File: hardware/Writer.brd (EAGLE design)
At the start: 68.6 x 53.3 mm, 20 parts, among them CN1 IRKit Wifi, IC1 JAPANINO-SLIM, SW1 SS12D01G4, SW2 SLIDE-SWITCH4/2

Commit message: SW2's pin4 wasn't connected to GND
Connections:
- removed net N$8: SW2.4
- net GND: now also SW2.4
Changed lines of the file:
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@@
 <via x="62.7" y="24.2" extent="1-16" drill="0.4"/>
 <via x="6.6" y="44.1" extent="1-16" drill="0.4"/>
+<contactref element="SW2" pad="4"/>
+<wire x1="62.95" y1="20.37" x2="62.7" y2="20.37" width="0.4064" layer="1"/>
 </signal>
 <signal name="VIN">
@@
 <contactref element="SW2" pad="2"/>
 </signal>
-<signal name="N$8">
-<contactref element="SW2" pad="4"/>
-</signal>
 <signal name="N$9">

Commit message: better error handling and logs preparing for factory-checker firmware POWER switch disconnects 5V and GND when turned off methods for factory checker test script follows main changes
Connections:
- new net N$8: SW1.3
- net GND: no longer SW1.3
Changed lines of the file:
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@@
 <contactref element="ICSP" pad="6"/>
 <contactref element="CN1" pad="8"/>
-<contactref element="SW1" pad="3"/>
 <contactref element="JP1" pad="1"/>
 <contactref element="LED2" pad="K"/>
@@
 <wire x1="7.1" y1="13.5" x2="7.05" y2="13.5" width="0.254" layer="1"/>
 </signal>
+<signal name="N$8">
+<contactref element="SW1" pad="3"/>
+</signal>
 </signals>

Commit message: looks fine
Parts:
- removed ICSP: IRKit ICSP, pinhead:2X03
- removed JP1: TTL-232R-3V3, pinhead:1X06/90
- removed LED2: OSG50805C1C, my:LED2012
- removed SW1: SS12D01G4, my:SS12D01G4
- removed SW2: SLIDE-SWITCH4/2, my:SLIDE-SWITCH-MCS421N
- added C1, C10, C11, C12, C3, C4, C5, C6: 0.1uF, my:SMD2012
- added C2: 10uF, my:PANASONIC_B
- added C7, C8: 12pF, my:SMD2012
- added C9: 1uF, my:SMD2012
- added CN2: TTL-232R-3V3, my:1X06/90
- added CN3: WiFi-Header, my:2X04
- added CN4: SOCKET-HEADER-7614-5002, my:SOCKET-HEADER-7614-5002
- added F1: MF-MSMF075-2, my:L1812
- added ICSP1: IRKit ICSP, my:2X03
- added ICSP2: Writer ICSP, my:2X03
- added R10, R11, R12, R13, R8: 1k, my:SMD2012
- added R9: 10k, my:SMD2012
- added SCREW1, SCREW2, SCREW3, SCREW4: flat-head M3 self-tapping, my:SCREW-M3
- added STANDOFF5, STANDOFF6, STANDOFF7: STAND-OFF, my:STAND-OFF
- added V1, V2, V3: CG0603MLC-05E, my:CT/CN0603
- added XTAL1: 16MHz CL:10pF, my:CRYSTAL-3.2-2.5
- CN1: value IRKit Wifi -> ZX62-B-5PA(11); device pinhead:2X04 -> my:USB-MICROB
- IC1: value JAPANINO-SLIM -> ATMEGA32U4AU; device my:JAPANINO-SLIM -> my:TQFP44-PAD
- R1: value 5.1k -> 22
- R2: value 1k -> 22
- R3: value 5.1k -> 1k
- R7: value 1k -> 5.1k
- moved STANDOFF1 61.5 mm to (49.0, 5.00)
- moved CN1 56.4 mm to (13.6, 54.5), turned to 180 degrees
- moved R2 47.3 mm to (10.7, 45.1), turned to 90 degrees
- moved STANDOFF4 45.0 mm to (5.00, 49.0)
- moved STANDOFF2 44.0 mm to (5.00, 5.00)
- moved R1 43.7 mm to (13.3, 45.1), turned to 90 degrees
- moved R4 38.5 mm to (42.0, 41.2), turned to 270 degrees
- moved IC1 36.7 mm to (24.9, 27.0), turned to 270 degrees
- moved LED1 34.6 mm to (27.8, 51.2), turned to 90 degrees
- moved R5 29.8 mm to (39.4, 41.2), turned to 270 degrees
- moved R6 29.6 mm to (34.4, 41.2), turned to 270 degrees
- moved R7 28.3 mm to (27.8, 46.6), turned to 90 degrees
- moved R3 19.3 mm to (44.6, 41.2), turned to 270 degrees
- moved U$1 17.2 mm to (36.3, 26.5)
- moved STANDOFF3 1.00 mm to (49.0, 49.0)
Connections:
- removed net 3V: IC1.3V
- removed net 5V: IC1.5V
- removed net MISO: IC1.D12, ICSP.1
- removed net MOSI: IC1.D11, ICSP.4
- removed net N$1: R6.1, SW2.1
- removed net N$10: R7.1, SW2.7
- removed net N$2: R3.1, SW2.C2
- removed net N$4: R2.1, SW2.C3
- removed net N$5: SW2.8
- removed net N$6: LED2.A, R3.2
- removed net N$7: SW2.2
- removed net N$8: SW1.3
- removed net N$9: SW2.6
- removed net RESET: IC1.D10, ICSP.5
- removed net SCK: IC1.D13, ICSP.3
- removed net VCC: CN1.7, ICSP.2, R1.1, SW1.2, SW2.3
- removed net VEXT: IC1.5V@2, SW1.1
- new net +5V: C1.1, C10.2, C11.2, C12.2, C2.+, C3.2, C4.2, C5.2, CN3.7, CN4.10, CN4.7, F1.2, IC1.14, IC1.2, IC1.24, IC1.34, IC1.44, IC1.7, ICSP1.2, ICSP2.2, R7.1, R9.2
- new net A0: IC1.36
- new net A1: IC1.37
- new net A2: IC1.38
- new net A3: IC1.39
- new net A4: IC1.40
- new net A5: IC1.41
- new net AREF: C6.2, IC1.42
- new net D0: IC1.20
- new net D1: IC1.21
- new net D10: IC1.30, R11.1
- new net D11: IC1.12, R10.1
- new net D12: IC1.26, R13.1
- new net D13: IC1.32, R12.1
- new net D2: IC1.19
- new net D3: IC1.18
- new net D4: IC1.25
- new net D5: IC1.31
- new net D6: IC1.27
- new net D7: IC1.1
- new net D8: IC1.28
- new net D9: IC1.29
- new net HWB: IC1.33
- new net IRKIT/!RESET: CN4.12, ICSP1.5, R11.2
- new net IRKIT/MISO: CN4.13, ICSP1.1, R13.2
- new net IRKIT/MOSI: CN4.14, ICSP1.4, R10.2
- new net IRKIT/SCK: CN4.9, ICSP1.3, R12.2
- new net N$48: CN1.P2, R1.2, V1.1
- new net N$51: CN1.P3, R2.2, V2.1
- new net N$52: CN1.P1, F1.1, V3.1
- new net RXLED: IC1.8
- new net TXLED: IC1.22
- new net UCAP: C9.2, IC1.6
- new net USB+: IC1.4, R2.1
- new net USB-: IC1.3, R1.1
- new net USB-ID: CN1.P4
- new net WRITER/!RESET: IC1.13, ICSP2.5, R9.1
- new net WRITER/MISO: IC1.11, ICSP2.1
- new net WRITER/MOSI: IC1.10, ICSP2.4
- new net WRITER/SCK: IC1.9, ICSP2.3
- new net XTAL1: C8.2, IC1.17, XTAL1.1
- new net XTAL2: C7.2, IC1.16, XTAL1.3
- net +3V3: now also CN3.1, CN4.2, R8.2; no longer CN1.1, R2.2
- net CTS#: now also CN2.2, R6.1; no longer JP1.2, R4.2
- net GND: now also C1.2, C10.1, C11.1, C12.1, C2.-, C3.1, C4.1, C5.1, C6.1, C7.1, C8.1, C9.1, CN1.P5, CN1.S1, CN1.S2, CN1.S3, CN1.S4, CN1.S5, CN1.S6, CN2.1, CN3.8, CN4.11, CN4.8, IC1.15, IC1.23, IC1.35, IC1.43, IC1.5, IC1.P$1, ICSP1.6, ICSP2.6, V1.2, V2.2, V3.2, XTAL1.2, XTAL1.4; no longer CN1.8, IC1.GND, IC1.GND1, IC1.GND2, ICSP.6, JP1.1, LED2.K, SW2.4
- net N$3: now also R7.2; no longer R1.2
- net RTS#: now also CN2.6, R3.1; no longer JP1.6, R5.2
- net RXD: now also CN2.5, R4.1; no longer JP1.5, R7.2
- net TXD: now also CN2.4, R5.1; no longer JP1.4, R6.2
- net VUSB: now also CN2.3; no longer JP1.3
- net WIFI_UART0_CTS: now also CN3.3, CN4.3, R3.2; no longer CN1.3, R5.1
- net WIFI_UART0_RTS: now also CN3.2, CN4.6, R6.2; no longer CN1.2, R4.1
- net WIFI_UART0_RX: now also CN3.5, CN4.4, R5.2; no longer CN1.5, SW2.C1
- net WIFI_UART0_TX: now also CN3.6, CN4.5, R4.2; no longer CN1.6, SW2.C4
- net WIFI_UART1_RTS: now also CN3.4, CN4.1, R8.1; no longer CN1.4, SW2.5
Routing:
- net +5V: track 0.00 -> 171.8 mm, vias 0 -> 3
- net VCC: track 109.7 -> 0.00 mm
- net VEXT: track 64.6 -> 0.00 mm
- net IRKIT/SCK: track 0.00 -> 63.3 mm
- net N$1: track 53.7 -> 0.00 mm
- net IRKIT/MISO: track 0.00 -> 52.7 mm
- net IRKIT/!RESET: track 0.00 -> 52.0 mm
- net N$10: track 46.1 -> 0.00 mm
- net IRKIT/MOSI: track 0.00 -> 41.9 mm
- net RESET: track 39.7 -> 0.00 mm
- net WIFI_UART0_TX: track 19.5 -> 57.7 mm
- net MOSI: track 33.5 -> 0.00 mm
- net MISO: track 32.5 -> 0.00 mm
- net SCK: track 31.9 -> 0.00 mm
- net WIFI_UART0_RX: track 18.2 -> 48.4 mm
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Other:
- board size 68.6 x 53.3 mm -> 54 x 56 mm
- board text added: "+3.3V"
- board text added: "+5V"
- board text added: "IRKit Writer2"
- board text removed: "CTS#"
- board text removed: "IRKit WRITER"
- board text removed: "POWER"
- board text removed: "PROGRAM"
- board text removed: "RTS#"
- board text removed: "RXD"
- board text removed: "TTL-232R-3V3"
- board text removed: "TXD"
- board text removed: "VUSB"
- board text removed: "Vcc"

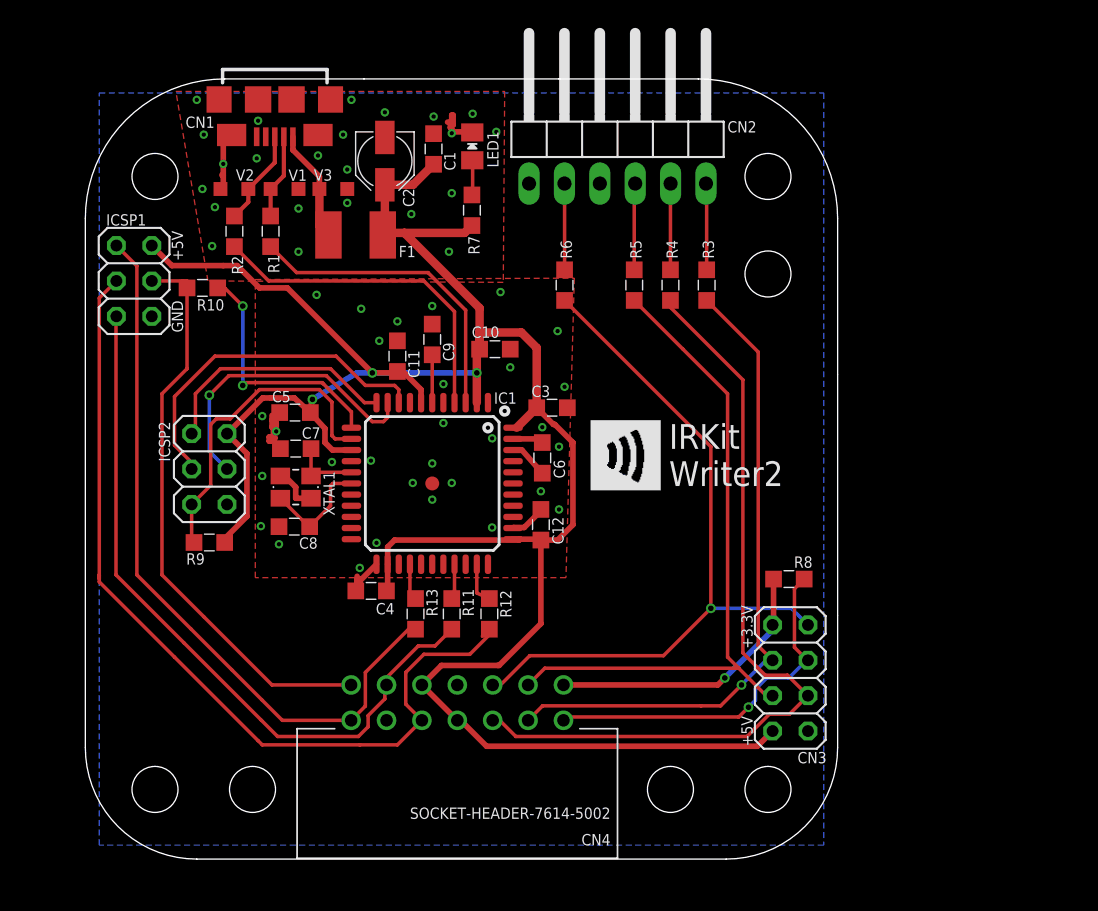
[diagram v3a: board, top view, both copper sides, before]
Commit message: added LED for ArduinoISP PMODE,ERR,HB. make ISP work on ATMEGA32U4.
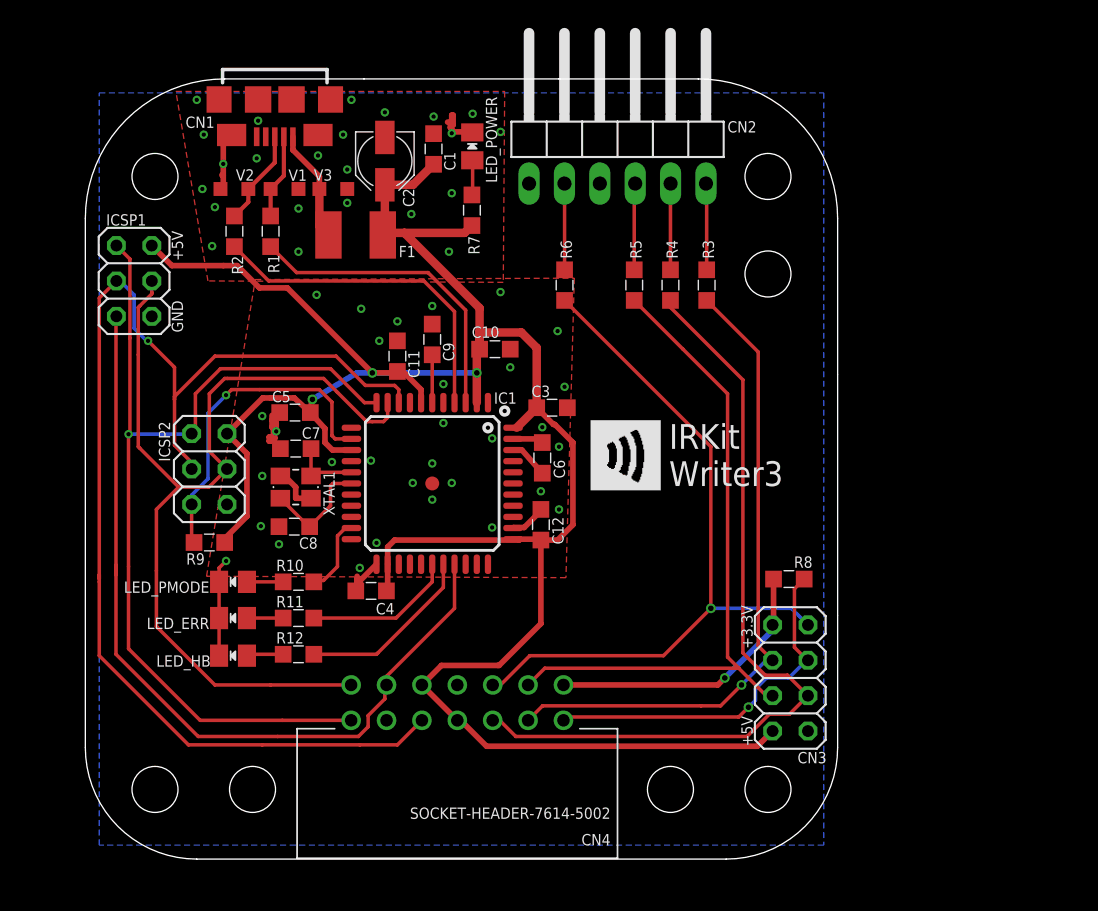
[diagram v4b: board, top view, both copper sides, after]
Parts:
- removed R13: 1k, my:SMD2012
- added LED_ERR, LED_HB, LED_PMODE: (no value), my:LED2012
- R10, R11, R12: value 1k -> 5.1k
- moved R10 22.2 mm to (15.3, 19.9)
- moved R12 14.0 mm to (15.3, 14.7), turned to 180 degrees
- moved R11 11.0 mm to (15.3, 17.3), turned to 180 degrees
- renumbered LED1 to LED_POWER
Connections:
- removed net D1: IC1.21
- removed net D10: IC1.30, R11.1
- removed net D8: IC1.28
- removed net D9: IC1.29
- removed net WRITER/MISO: IC1.11, ICSP2.1
- removed net WRITER/MOSI: IC1.10, ICSP2.4
- removed net WRITER/SCK: IC1.9, ICSP2.3
- new net D1/LED_PMODE: IC1.21, R10.1
- new net D8/LED_ERR: IC1.28, R11.1
- new net D9/LED_HB: IC1.29, R12.1
- new net N$1: LED_PMODE.A, R10.2
- new net N$2: LED_ERR.A, R11.2
- new net N$4: LED_HB.A, R12.2
- net D11: no longer R10.1
- net D12: no longer R13.1
- net D13: no longer R12.1
- net GND: now also LED_ERR.K, LED_HB.K, LED_PMODE.K
- net IRKIT/!RESET: now also IC1.30; no longer R11.2
- net IRKIT/MISO: now also IC1.11, ICSP2.1; no longer R13.2
- net IRKIT/MOSI: now also IC1.10, ICSP2.4; no longer R10.2
- net IRKIT/SCK: now also IC1.9, ICSP2.3; no longer R12.2
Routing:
- net IRKIT/MOSI: track 41.9 -> 68.6 mm
- net IRKIT/SCK: track 63.3 -> 89.6 mm, vias 0 -> 1
- net WRITER/SCK: track 24.9 -> 0.00 mm
- net WRITER/MOSI: track 21.8 -> 0.00 mm, vias 1 -> 0
- net D11: track 17.9 -> 0.00 mm, vias 2 -> 0
- net WRITER/MISO: track 17.7 -> 0.00 mm
- net IRKIT/MISO: track 52.7 -> 69.8 mm, vias 0 -> 1
- net D9/LED_HB: track 0.00 -> 13.0 mm
- net D8/LED_ERR: track 0.00 -> 10.8 mm
- net IRKIT/!RESET: track 52.0 -> 60.2 mm
- net GND: track 26.1 -> 33.1 mm, vias 53 -> 54
- net D1/LED_PMODE: track 0.00 -> 5.63 mm
- net D13: track 3.05 -> 0.00 mm
- net N$4: track 0.00 -> 2.70 mm
- net D12: track 2.63 -> 0.00 mm
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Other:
- board text added: "IRKit Writer3"
- board text removed: "IRKit Writer2"
